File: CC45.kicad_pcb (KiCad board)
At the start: 2 copper layers, 247 x 80.8 mm, 128 parts, among them J1 AVR-ISP-6, SW1 RESET, SW10 K08, SW11 K09, SW12 K0A, SW13 K0B, SW14 K0C, SW15 K10, SW16 K11, SW17 K12, SW18 K13, SW19 K14, SW2 K00, SW20 K15, SW21 K16, SW22 K17, SW23 K18, SW24 K19, SW25 K1A, SW26 K1B, SW27 K20, SW28 K21, SW29 K22, SW3 K01, SW30 K23, SW31 K24, SW32 K25, SW33 K26, SW34 K27, SW35 K28, SW36 K29, SW37 K2A, SW38 K2B, SW39 K30, SW4 K02, SW40 K31, SW41 K32, SW42 K33, SW43 K34, SW44 K36, SW45 K38, SW46 K39, SW47 K3A, SW48 K3B, SW5 K03, SW6 K04, SW7 K05, SW8 K06, SW9 K07, U1 ATmega32U4-AU, U2 PRTR5V0U2X, X1 XTAL

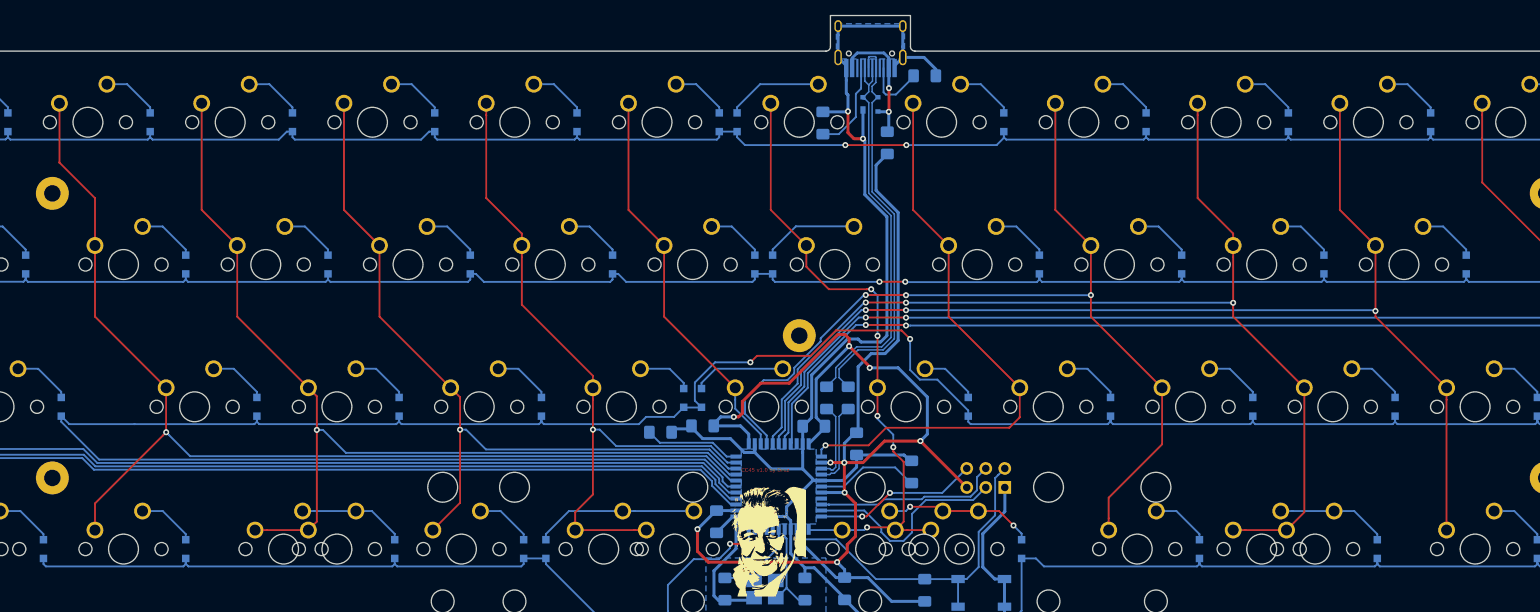
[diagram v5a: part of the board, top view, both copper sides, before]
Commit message: added the 1u keys for the 1.5u bottom row option
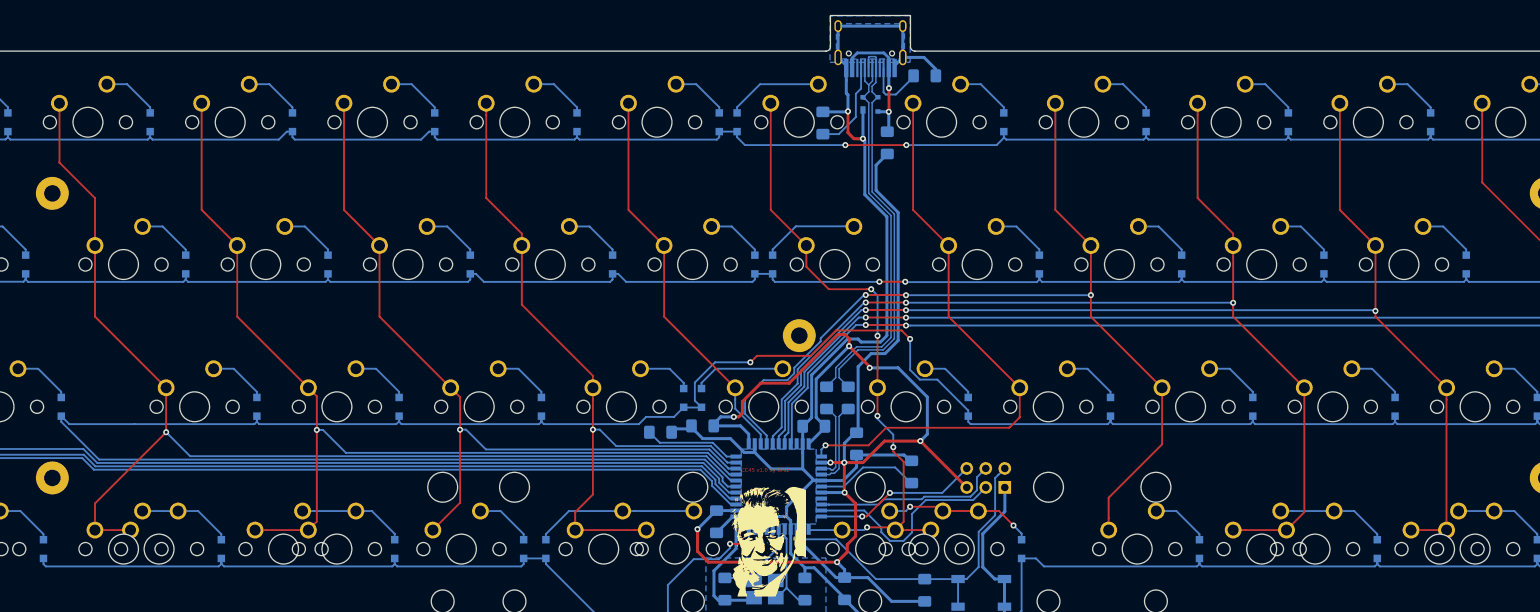
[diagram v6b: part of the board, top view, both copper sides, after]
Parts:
- added SW40: K31, MX_19mm:MX_19mm-1U-NoLED, F.Cu at (61.8, 90.2)
- added SW47: K3A, MX_19mm:MX_19mm-1U-NoLED, F.Cu at (232.8, 90.2)
- moved D39 4.75 mm to (70.1, 90.2)
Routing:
- net col10: track 154.0 -> 158.8 mm
- net col1: track 145.6 -> 150.4 mm
- net Net-(D46-Pad2): track 7.80 -> 12.5 mm
- net Net-(D39-Pad2): track 7.80 -> 12.5 mm
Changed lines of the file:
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@@
     (thickness 1.6)
     (drawings 17)
-    (tracks 1011)
+    (tracks 1015)
     (zones 0)
-    (modules 128)
+    (modules 130)
     (nets 90)
   )
@@
     (35 F.Paste user)
     (36 B.SilkS user)
-    (37 F.SilkS user)
+    (37 F.SilkS user hide)
     (38 B.Mask user)
     (39 F.Mask user)
@@
     (add_net VCC)
   )
+  (module MX_19mm:MX_19mm-1U-NoLED (layer F.Cu)
+    (at 61.75 90.25)
+    (fp_text reference SW40 (at 0 3.175) (layer Dwgs.User)
+      (effects (font (size 1 1) (thickness 0.15)))
+    )
+    (fp_text value K31 (at 0 -7.9375) (layer Dwgs.User)
+      (effects (font (size 1 1) (thickness 0.15)))
+    )
+    (fp_line (start -9.5 9.5) (end -9.5 -9.5) (layer Dwgs.User) (width 0.15))
+    (fp_line (start 9.5 9.5) (end -9.5 9.5) (layer Dwgs.User) (width 0.15))
+    (fp_line (start 9.5 -9.5) (end 9.5 9.5) (layer Dwgs.User) (width 0.15))
+    (fp_line (start -9.5 -9.5) (end 9.5 -9.5) (layer Dwgs.User) (width 0.15))
+    (fp_line (start -7 -7) (end -7 -5) (layer Dwgs.User) (width 0.15))
+    (fp_line (start -5 -7) (end -7 -7) (layer Dwgs.User) (width 0.15))
+    (fp_line (start -7 7) (end -5 7) (layer Dwgs.User) (width 0.15))
+    (fp_line (start -7 5) (end -7 7) (layer Dwgs.User) (width 0.15))
+    (fp_line (start 7 7) (end 7 5) (layer Dwgs.User) (width 0.15))
+    (fp_line (start 5 7) (end 7 7) (layer Dwgs.User) (width 0.15))
+    (fp_line (start 7 -7) (end 7 -5) (layer Dwgs.User) (width 0.15))
+    (fp_line (start 5 -7) (end 7 -7) (layer Dwgs.User) (width 0.15))
+    (pad "" np_thru_hole circle (at 5.08 0 48.0996) (size 1.75 1.75) (drill 1.75) (layers *.Cu *.Mask))
+    (pad "" np_thru_hole circle (at -5.08 0 48.0996) (size 1.75 1.75) (drill 1.75) (layers *.Cu *.Mask))
+    (pad 2 thru_hole circle (at -3.81 -2.54) (size 2.25 2.25) (drill 1.47) (layers *.Cu B.Mask)
+      (net 68 col1))
+    (pad "" np_thru_hole circle (at 0 0) (size 3.9878 3.9878) (drill 3.9878) (layers *.Cu *.Mask))
+    (pad 1 thru_hole circle (at 2.54 -5.08) (size 2.25 2.25) (drill 1.47) (layers *.Cu B.Mask)
+      (net 48 "Net-(D39-Pad2)"))
+  )
+  (module MX_19mm:MX_19mm-1U-NoLED (layer F.Cu)
+    (at 232.75 90.25)
+    (fp_text reference SW47 (at 0 3.175) (layer Dwgs.User)
+      (effects (font (size 1 1) (thickness 0.15)))
+    )
+    (fp_text value K3A (at 0 -7.9375) (layer Dwgs.User)
+      (effects (font (size 1 1) (thickness 0.15)))
+    )
+    (fp_line (start -9.5 9.5) (end -9.5 -9.5) (layer Dwgs.User) (width 0.15))
+    (fp_line (start 9.5 9.5) (end -9.5 9.5) (layer Dwgs.User) (width 0.15))
+    (fp_line (start 9.5 -9.5) (end 9.5 9.5) (layer Dwgs.User) (width 0.15))
+    (fp_line (start -9.5 -9.5) (end 9.5 -9.5) (layer Dwgs.User) (width 0.15))
+    (fp_line (start -7 -7) (end -7 -5) (layer Dwgs.User) (width 0.15))
+    (fp_line (start -5 -7) (end -7 -7) (layer Dwgs.User) (width 0.15))
+    (fp_line (start -7 7) (end -5 7) (layer Dwgs.User) (width 0.15))
+    (fp_line (start -7 5) (end -7 7) (layer Dwgs.User) (width 0.15))
+    (fp_line (start 7 7) (end 7 5) (layer Dwgs.User) (width 0.15))
+    (fp_line (start 5 7) (end 7 7) (layer Dwgs.User) (width 0.15))
+    (fp_line (start 7 -7) (end 7 -5) (layer Dwgs.User) (width 0.15))
+    (fp_line (start 5 -7) (end 7 -7) (layer Dwgs.User) (width 0.15))
+    (pad "" np_thru_hole circle (at 5.08 0 48.0996) (size 1.75 1.75) (drill 1.75) (layers *.Cu *.Mask))
+    (pad "" np_thru_hole circle (at -5.08 0 48.0996) (size 1.75 1.75) (drill 1.75) (layers *.Cu *.Mask))
+    (pad 2 thru_hole circle (at -3.81 -2.54) (size 2.25 2.25) (drill 1.47) (layers *.Cu B.Mask)
+      (net 77 col10))
+    (pad "" np_thru_hole circle (at 0 0) (size 3.9878 3.9878) (drill 3.9878) (layers *.Cu *.Mask))
+    (pad 1 thru_hole circle (at 2.54 -5.08) (size 2.25 2.25) (drill 1.47) (layers *.Cu B.Mask)
+      (net 55 "Net-(D46-Pad2)"))
+  )
   (module MountingHole:MountingHole_2.2mm_M2_Pad (layer F.Cu)
     (at 147.25 61.75)
@@
   )
   (module custom:D_SOD-323_HandSoldering (layer B.Cu)
-    (at 65.3125 90.25 90)
+    (at 70.0625 90.25 90)
     (descr SOD-323)
     (tags SOD-323)
@@
   (segment (start 110.118599 92.568901) (end 110.4375 92.25) (width 0.25) (layer B.Cu) (net 47))
   (segment (start 110.4375 92.25) (end 110.4375 91.5) (width 0.25) (layer B.Cu) (net 47))
-  (segment (start 65.3125 92.2125) (end 65.668901 92.568901) (width 0.25) (layer B.Cu) (net 47))
-  (segment (start 65.3125 91.5) (end 65.3125 92.2125) (width 0.25) (layer B.Cu) (net 47))
-  (segment (start 65.668901 92.568901) (end 92.899849 92.568901) (width 0.25) (layer B.Cu) (net 47))
-  (segment (start 92.899849 92.568901) (end 93.21875 92.25) (width 0.25) (layer B.Cu) (net 47))
-  (segment (start 46.3125 91.5) (end 46.3125 92.25) (width 0.25) (layer B.Cu) (net 47))
-  (segment (start 46.3125 92.25) (end 46.631401 92.568901) (width 0.25) (layer B.Cu) (net 47))
-  (segment (start 46.631401 92.568901) (end 64.993599 92.568901) (width 0.25) (layer B.Cu) (net 47))
-  (segment (start 64.993599 92.568901) (end 65.3125 92.25) (width 0.25) (layer B.Cu) (net 47))
-  (segment (start 65.3125 92.25) (end 65.3125 91.5) (width 0.25) (layer B.Cu) (net 47))
   (segment (start 129.7 98.509299) (end 129.7 99.074984) (width 0.25) (layer B.Cu) (net 47))
   (segment (start 138 90.115685) (end 136.515685 91.6) (width 0.25) (layer B.Cu) (net 47))
@@
   (segment (start 133.15 91.6) (end 129.7 95.05) (width 0.25) (layer B.Cu) (net 47))
   (segment (start 129.7 95.05) (end 129.7 98.509299) (width 0.25) (layer B.Cu) (net 47))
-  (segment (start 59.54 85.17) (end 62.2325 85.17) (width 0.25) (layer B.Cu) (net 48))
-  (segment (start 62.2325 85.17) (end 65.3125 88.25) (width 0.25) (layer B.Cu) (net 48))
-  (segment (start 65.3125 88.25) (end 65.3125 89) (width 0.25) (layer B.Cu) (net 48))
+  (segment (start 69.731099 92.568901) (end 70.0625 92.2375) (width 0.25) (layer B.Cu) (net 47))
+  (segment (start 70.0625 92.2375) (end 70.0625 91.5) (width 0.25) (layer B.Cu) (net 47))
+  (segment (start 46.631401 92.568901) (end 69.731099 92.568901) (width 0.25) (layer B.Cu) (net 47))
+  (segment (start 46.3125 91.5) (end 46.3125 92.25) (width 0.25) (layer B.Cu) (net 47))
+  (segment (start 46.3125 92.25) (end 46.631401 92.568901) (width 0.25) (layer B.Cu) (net 47))
+  (segment (start 70.418901 92.568901) (end 70.0625 92.2125) (width 0.25) (layer B.Cu) (net 47))
+  (segment (start 70.0625 92.2125) (end 70.0625 91.5) (width 0.25) (layer B.Cu) (net 47))
+  (segment (start 93.21875 92.25) (end 92.899849 92.568901) (width 0.25) (layer B.Cu) (net 47))
+  (segment (start 92.899849 92.568901) (end 70.418901 92.568901) (width 0.25) (layer B.Cu) (net 47))
+  (segment (start 59.54 85.17) (end 64.29 85.17) (width 0.25) (layer B.Cu) (net 48))
+  (segment (start 70.0625 88.2625) (end 70.0625 89) (width 0.25) (layer B.Cu) (net 48))
+  (segment (start 64.29 85.17) (end 66.97 85.17) (width 0.25) (layer B.Cu) (net 48))
+  (segment (start 66.97 85.17) (end 70.0625 88.2625) (width 0.25) (layer B.Cu) (net 48))
   (segment (start 90.17 85.17) (end 93.21875 88.21875) (width 0.25) (layer B.Cu) (net 49))
   (segment (start 88.04 85.17) (end 90.17 85.17) (width 0.25) (layer B.Cu) (net 49))
@@
   (segment (start 242.7325 85.17) (end 245.8125 88.25) (width 0.25) (layer B.Cu) (net 55))
   (segment (start 245.8125 88.25) (end 245.8125 89) (width 0.25) (layer B.Cu) (net 55))
+  (segment (start 235.29 85.17) (end 240.04 85.17) (width 0.25) (layer B.Cu) (net 55))
   (segment (start 261.415 85.17) (end 264.1075 85.17) (width 0.25) (layer B.Cu) (net 56))
   (segment (start 264.1075 85.17) (end 267.1875 88.25) (width 0.25) (layer B.Cu) (net 56))
@@
   (segment (start 48.44 30.71) (end 48.44 38.64) (width 0.25) (layer F.Cu) (net 68))
   (segment (start 48.44 38.64) (end 53.19 43.39) (width 0.25) (layer F.Cu) (net 68))
+  (segment (start 53.19 87.71) (end 57.94 87.71) (width 0.25) (layer F.Cu) (net 68))
   (segment (start 82.814999 69.834999) (end 81.69 68.71) (width 0.25) (layer F.Cu) (net 69))
   (segment (start 82.814999 74.335001) (end 82.814999 69.834999) (width 0.25) (layer F.Cu) (net 69))
@@
   (segment (start 144.5 76.2) (end 144.5 75.2) (width 0.25) (layer B.Cu) (net 77))
   (segment (start 155.55971 58.324994) (end 156.125 58.324994) (width 0.25) (layer B.Cu) (net 77))
+  (segment (start 228.94 87.71) (end 233.69 87.71) (width 0.25) (layer F.Cu) (net 77))
   (segment (start 250.315 63.96) (end 250.315 59.900685) (width 0.25) (layer F.Cu) (net 78))
   (segment (start 250.315 59.900685) (end 250.315 59.335) (width 0.25) (layer F.Cu) (net 78))
@@
       )
     )
+  )
+  (zone (net 1) (net_name GND) (layer B.Cu) (hatch edge 0.508)
+    (connect_pads (clearance 0.508))
+    (min_thickness 0.254)
+    (fill yes (arc_segments 32) (thermal_gap 0.508) (thermal_bridge_width 0.508))
+    (polygon
+      (pts
+        (xy 151.35 19.05) (xy 151.35 25.25) (xy 162.05 25.25) (xy 162.05 19)
+      )
+    )

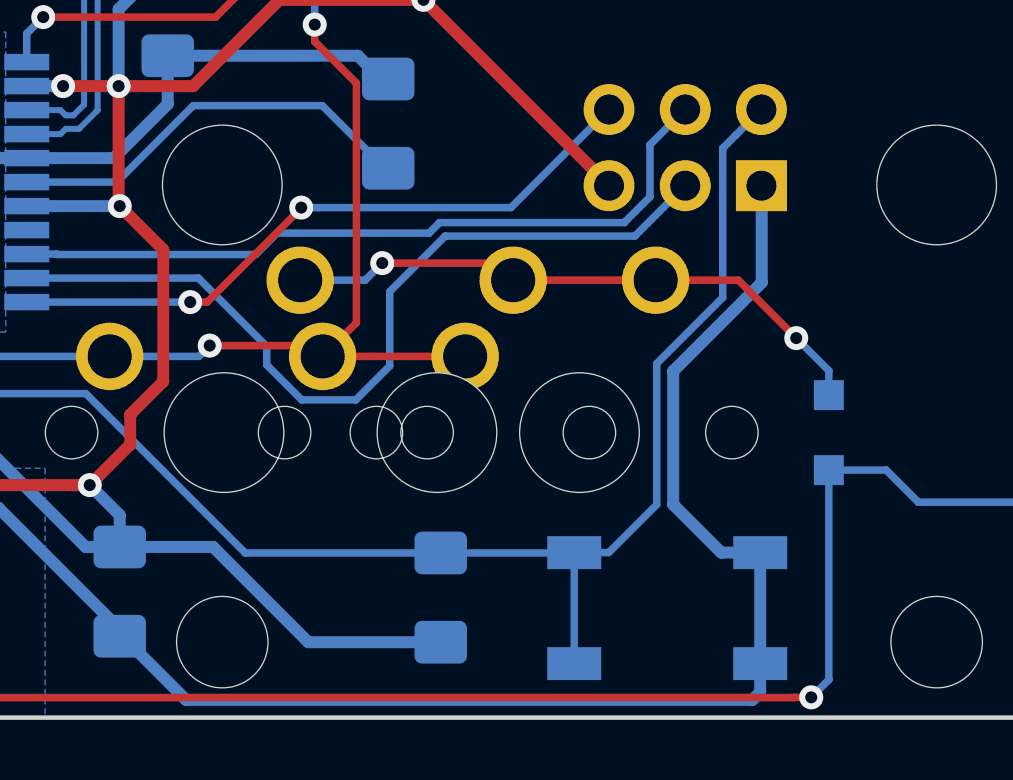
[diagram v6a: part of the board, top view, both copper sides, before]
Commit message: fix reset button wiring
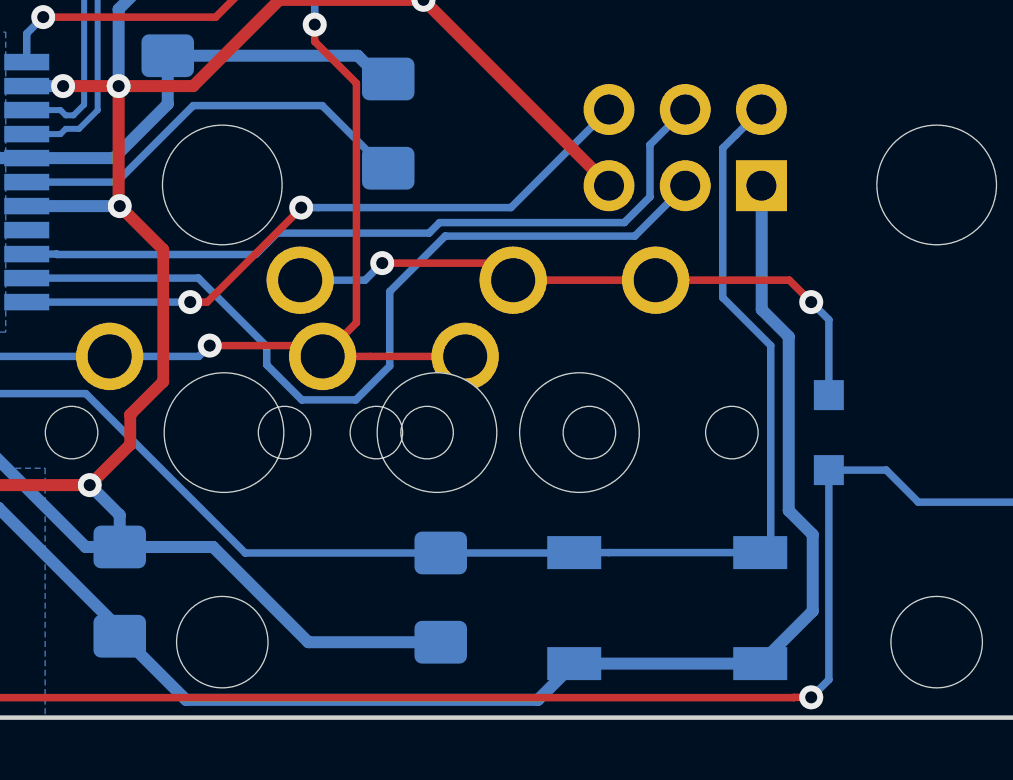
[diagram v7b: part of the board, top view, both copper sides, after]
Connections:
- SW1 pad 1: GND -> RESET
- SW1 pad 2: RESET -> GND
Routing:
- net GND: track 236.5 -> 234.2 mm
- net Net-(D43-Pad2): track 20.2 -> 21.2 mm
- net RESET: track 45.8 -> 46.4 mm

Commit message: Updated version number on pcb
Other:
- board text added: "CC45 v1.1 by Druz github.com/aaarsene/CC45"
- board text removed: "CC45 v1.0 by Druz"
